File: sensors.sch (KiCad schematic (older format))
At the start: 4 parts

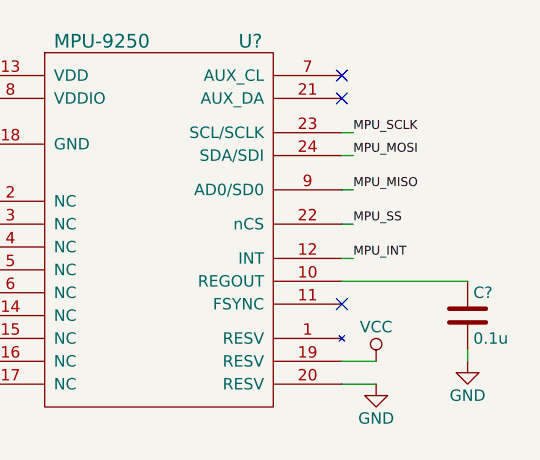
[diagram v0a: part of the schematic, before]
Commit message: Adjust MPU9250 wiring to MCU
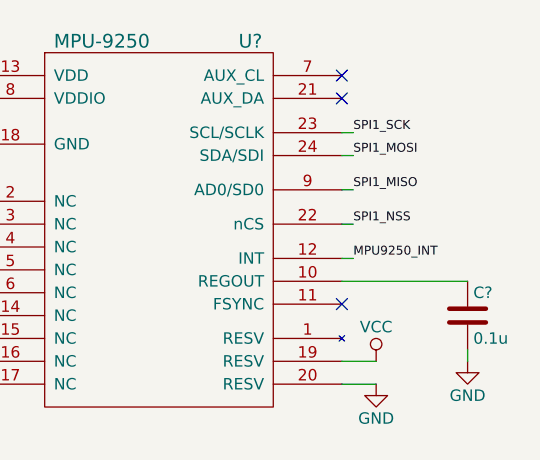
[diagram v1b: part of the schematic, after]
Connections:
- net MPU_INT renamed MPU9250_INT
- net MPU_MISO renamed SPI1_MISO
- net MPU_MOSI renamed SPI1_MOSI
- net MPU_SCLK renamed SPI1_SCK
- net MPU_SS renamed SPI1_NSS
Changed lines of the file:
@@
 $EndComp
 Text Label 3750 1950 0    39   ~ 0
-MPU_MISO
+SPI1_MISO
 Wire Wire Line
 	2100 2800 1900 2800
@@
 	3750 1950 3700 1950
 Text Label 3750 2100 0    39   ~ 0
-MPU_SS
+SPI1_NSS
 Wire Wire Line
 	3750 2100 3700 2100
 Text Label 3750 1800 0    39   ~ 0
-MPU_MOSI
+SPI1_MOSI
 Text Label 3750 1700 0    39   ~ 0
-MPU_SCLK
+SPI1_SCK
 Wire Wire Line
 	3750 1800 3700 1800
@@
 NoConn ~ 3700 2450
 Text Label 3750 2250 0    39   ~ 0
-MPU_INT
+MPU9250_INT
 Wire Wire Line
 	3750 2250 3700 2250

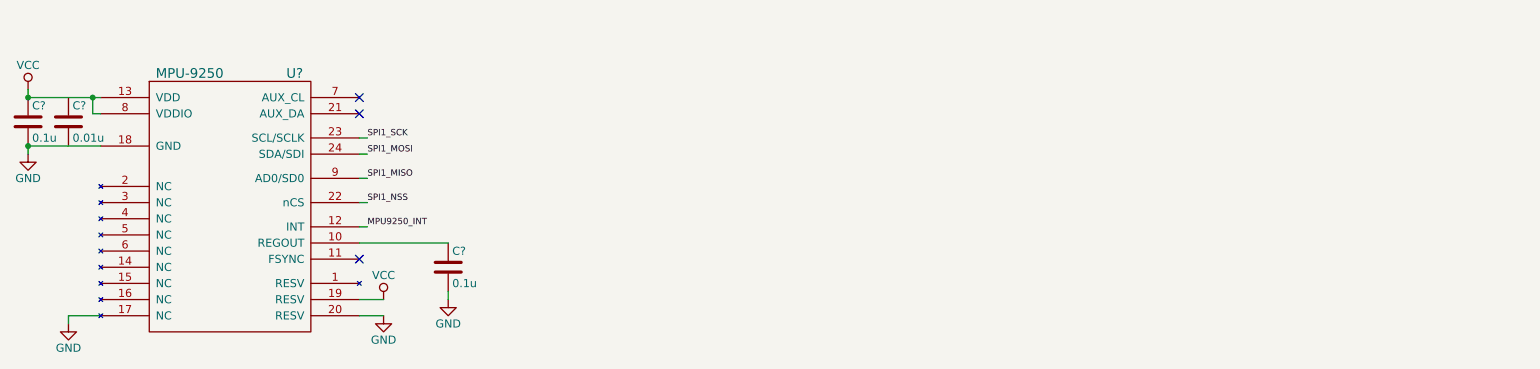
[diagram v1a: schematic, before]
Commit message: Add ground sensor (VL6180X)
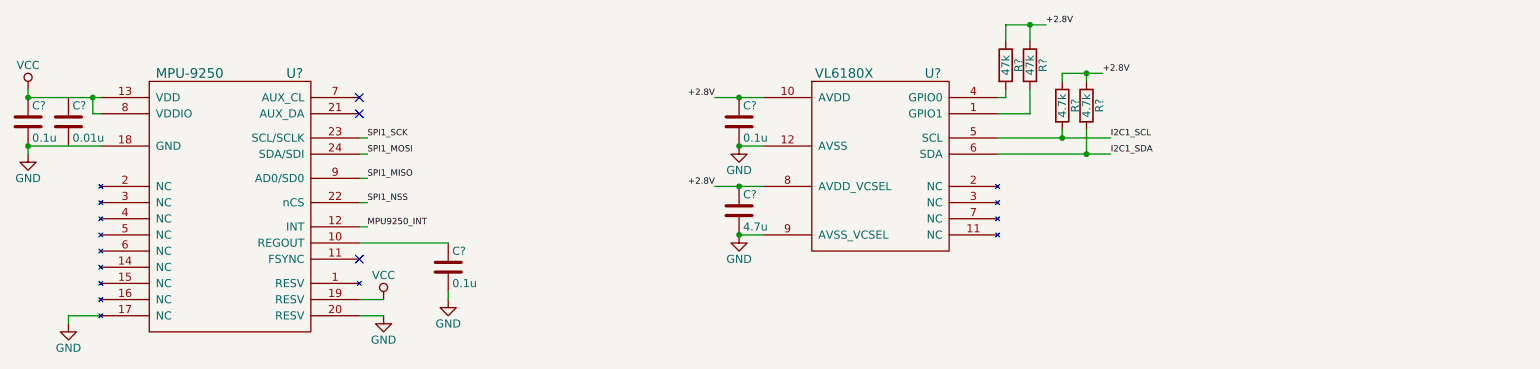
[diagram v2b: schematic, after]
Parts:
- added C?: 4.7u, symbol C
- added C?: 0.1u, symbol C
- added R? (x2): 47k, symbol R
- added R? (x2): 4.7k, symbol R
- added U?: VL6180X, symbol VL6180X
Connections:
- net GND: now also C?.2, C?.2, U?.12 (AVSS), U?.9 (AVSS_VCSEL)
- new net: R?.2, U?.4 (GPIO0)
- new net: R?.2, U?.1 (GPIO1)
- new net +2.8V: C?.1, C?.1, R?.1, R?.1, R?.1, R?.1, U?.10 (AVDD), U?.8 (AVDD_VCSEL)
- new net I2C1_SCL: R?.2, U?.5 (SCL)
- new net I2C1_SDA: R?.2, U?.6 (SDA)
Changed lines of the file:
@@
 Text Label 3750 1950 0    39   ~ 0
 SPI1_MISO
-Wire Wire Line
-	2100 2800 1900 2800
-Wire Wire Line
-	1900 2800 1900 2850
-Wire Wire Line
-	1650 1450 2100 1450
-Wire Wire Line
-	1650 1750 2100 1750
-Wire Wire Line
-	1650 1450 1650 1400
-Wire Wire Line
-	1650 1750 1650 1800
-Connection ~ 1650 1750
-Connection ~ 1650 1450
-Connection ~ 2050 1450
-Wire Wire Line
-	2100 1550 2050 1550
-Wire Wire Line
-	2050 1550 2050 1450
-Wire Wire Line
-	4250 2700 4250 2650
-Wire Wire Line
-	4250 2350 3700 2350
-Wire Wire Line
-	3750 1950 3700 1950
 Text Label 3750 2100 0    39   ~ 0
 SPI1_NSS
-Wire Wire Line
-	3750 2100 3700 2100
 Text Label 3750 1800 0    39   ~ 0
 SPI1_MOSI
 Text Label 3750 1700 0    39   ~ 0
 SPI1_SCK
-Wire Wire Line
-	3750 1800 3700 1800
-Wire Wire Line
-	3750 1700 3700 1700
 NoConn ~ 3700 1450
 NoConn ~ 3700 1550
@@
 Text Label 3750 2250 0    39   ~ 0
 MPU9250_INT
-Wire Wire Line
-	3750 2250 3700 2250
 $Comp
 L MPU-9250 U?
@@
 	1    0    0    -1
 $EndComp
+Text Label 5900 1450 2    39   ~ 0
++2.8V
+Text Label 5900 2000 2    39   ~ 0
++2.8V
+Wire Wire Line
+	2100 2800 1900 2800
+Wire Wire Line
+	1900 2800 1900 2850
+Wire Wire Line
+	1650 1450 2050 1450
+Wire Wire Line
+	2050 1450 2100 1450
+Wire Wire Line
+	1650 1750 2100 1750
+Wire Wire Line
+	1650 1450 1650 1400
+Wire Wire Line
+	1650 1750 1650 1800
+Connection ~ 1650 1750
+Connection ~ 1650 1450
+Connection ~ 2050 1450
+Wire Wire Line
+	2100 1550 2050 1550
+Wire Wire Line
+	2050 1550 2050 1450
+Wire Wire Line
+	4250 2700 4250 2650
+Wire Wire Line
+	4250 2350 3700 2350
+Wire Wire Line
+	3750 1950 3700 1950
+Wire Wire Line
+	3750 2100 3700 2100
+Wire Wire Line
+	3750 1800 3700 1800
+Wire Wire Line
+	3750 1700 3700 1700
+Wire Wire Line
+	3750 2250 3700 2250
 Wire Wire Line
 	3850 2800 3700 2800
 Wire Wire Line
 	3700 2700 3850 2700
+Wire Wire Line
+	5900 1450 6050 1450
+Wire Wire Line
+	6050 1450 6200 1450
+Wire Wire Line
+	5900 2000 6050 2000
+Wire Wire Line
+	6050 2000 6200 2000
+$Comp
+L C C?
+U 1 1 5536FB84
+P 6050 2150
+F 0 "C?" H 6075 2250 50  0000 L CNN
+F 1 "4.7u" H 6075 2050 50  0000 L CNN
+F 2 "" H 6088 2000 30  0000 C CNN
+F 3 "" H 6050 2150 60  0000 C CNN
+	1    6050 2150
+	1    0    0    -1
+$EndComp
+Wire Wire Line
+	6050 2300 6200 2300
+$Comp
+L GND #PWR?
+U 1 1 5536FBED
+P 6050 2300
+F 0 "#PWR?" H 6050 2050 50  0001 C CNN
+F 1 "GND" H 6050 2150 50  0000 C CNN
+F 2 "" H 6050 2300 60  0000 C CNN
+F 3 "" H 6050 2300 60  0000 C CNN
+	1    6050 2300
+	1    0    0    -1
+$EndComp
+$Comp
+L GND #PWR?
+U 1 1 5536FC2A
+P 6050 1750
+F 0 "#PWR?" H 6050 1500 50  0001 C CNN
+F 1 "GND" H 6050 1600 50  0000 C CNN
+F 2 "" H 6050 1750 60  0000 C CNN
+F 3 "" H 6050 1750 60  0000 C CNN
+	1    6050 1750
+	1    0    0    -1
+$EndComp
+Connection ~ 6050 2300
+Connection ~ 6050 2000
+$Comp
+L C C?
+U 1 1 5536FC5F
+P 6050 1600
+F 0 "C?" H 6075 1700 50  0000 L CNN
+F 1 "0.1u" H 6075 1500 50  0000 L CNN
+F 2 "" H 6088 1450 30  0000 C CNN
+F 3 "" H 6050 1600 60  0000 C CNN
+	1    6050 1600
+	1    0    0    -1
+$EndComp
+Wire Wire Line
+	6200 1750 6050 1750
+Connection ~ 6050 1750
+Connection ~ 6050 1450
+$Comp
+L R R?
+U 1 1 5536FCF9
+P 7700 1250
+F 0 "R?" V 7780 1250 50  0000 C CNN
+F 1 "47k" V 7700 1250 50  0000 C CNN
+F 2 "" V 7630 1250 30  0000 C CNN
+F 3 "" H 7700 1250 30  0000 C CNN
+	1    7700 1250
+	1    0    0    -1
+$EndComp
+$Comp
+L R R?
+U 1 1 5536FD36
+P 7850 1250
+F 0 "R?" V 7930 1250 50  0000 C CNN
+F 1 "47k" V 7850 1250 50  0000 C CNN
+F 2 "" V 7780 1250 30  0000 C CNN
+F 3 "" H 7850 1250 30  0000 C CNN
+	1    7850 1250
+	1    0    0    -1
+$EndComp
+Text Label 7950 1000 0    39   ~ 0
++2.8V
+Wire Wire Line
+	7700 1000 7850 1000
+Wire Wire Line
+	7850 1000 7950 1000
+Wire Wire Line
+	7850 1000 7850 1100
+Wire Wire Line
+	7700 1000 7700 1100
+Connection ~ 7850 1000
+Wire Wire Line
+	7650 1450 7700 1450
+Wire Wire Line
+	7650 1550 7850 1550
+Wire Wire Line
+	7850 1550 7850 1400
+Text Label 8300 1300 0    39   ~ 0
++2.8V
+$Comp
+L R R?
+U 1 1 5536FF70
+P 8200 1500
+F 0 "R?" V 8280 1500 50  0000 C CNN
+F 1 "4.7k" V 8200 1500 50  0000 C CNN
+F 2 "" V 8130 1500 30  0000 C CNN
+F 3 "" H 8200 1500 30  0000 C CNN
+	1    8200 1500
+	1    0    0    -1
+$EndComp
+Wire Wire Line
+	8050 1300 8200 1300
+Wire Wire Line
+	8200 1300 8300 1300
+Wire Wire Line
+	8200 1300 8200 1350
+Wire Wire Line
+	8050 1300 8050 1350
+Connection ~ 8200 1300
+Wire Wire Line
+	8050 1650 8050 1700
+Wire Wire Line
+	7650 1700 8050 1700
+Wire Wire Line
+	8050 1700 8350 1700
+Wire Wire Line
+	7650 1800 8200 1800
+Wire Wire Line
+	8200 1800 8350 1800
+Wire Wire Line
+	8200 1800 8200 1650
+Wire Wire Line
+	7700 1450 7700 1400
+Text Label 8350 1700 0    39   ~ 0
+I2C1_SCL
+Text Label 8350 1800 0    39   ~ 0
+I2C1_SDA
+Connection ~ 8200 1800
+Connection ~ 8050 1700
+$Comp
+L VL6180X U?
+U 1 1 553709E6
+P 6600 1700
+F 0 "U?" H 7250 2100 59  0000 C CNN
+F 1 "VL6180X" H 6700 2100 59  0000 C CNN
+F 2 "" H 6800 2300 39  0000 C CNN
+F 3 "" H 6800 2300 39  0000 C CNN
+	1    6600 1700
+	1    0    0    -1
+$EndComp
+$Comp
+L R R?
+U 1 1 5536FEA0
+P 8050 1500
+F 0 "R?" V 8130 1500 50  0000 C CNN
+F 1 "4.7k" V 8050 1500 50  0000 C CNN
+F 2 "" V 7980 1500 30  0000 C CNN
+F 3 "" H 8050 1500 30  0000 C CNN
+	1    8050 1500
+	1    0    0    -1
+$EndComp
 $EndSCHEMATC

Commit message: Add level shifters for i2c of TOF sensor
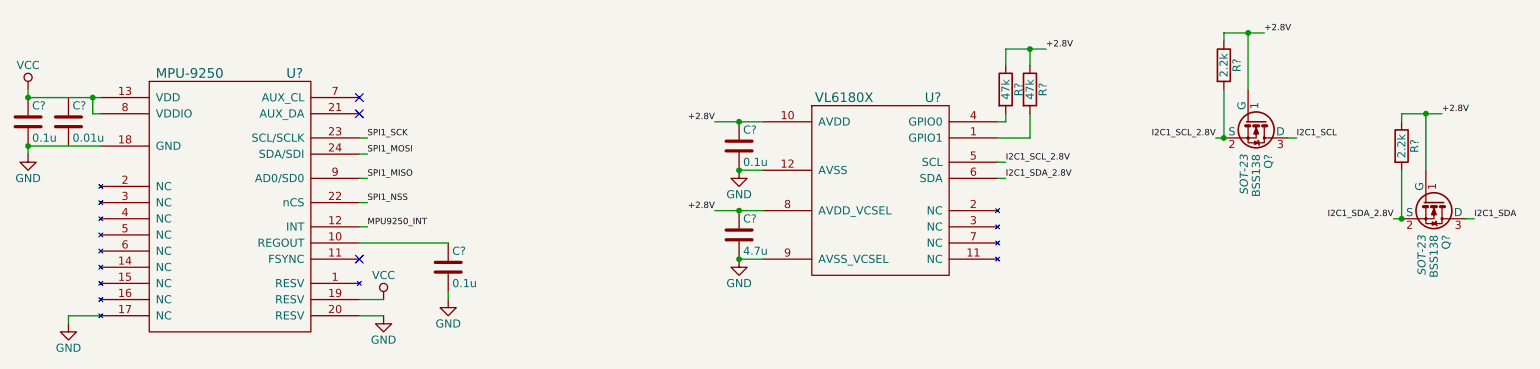
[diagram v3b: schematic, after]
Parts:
- added Q? (x2): BSS138, SOT-23, symbol BSS138
- R? (x2): value 4.7k -> 2.2k
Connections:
- net +2.8V: now also Q?.1 (G), Q?.1 (G)
- net I2C1_SCL: now also Q?.3 (D); no longer R?.2, U?.5 (SCL)
- net I2C1_SDA: now also Q?.3 (D); no longer R?.2, U?.6 (SDA)
- new net I2C1_SCL_2.8V: Q?.2 (S), R?.2, U?.5 (SCL)
- new net I2C1_SDA_2.8V: Q?.2 (S), R?.2, U?.6 (SDA)
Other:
- moved on the sheet: C?, R?, U?
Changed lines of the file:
@@
 	1    0    0    -1
 $EndComp
-Text Label 5900 1450 2    39   ~ 0
-+2.8V
-Text Label 5900 2000 2    39   ~ 0
+Text Label 5900 1600 2    39   ~ 0
++2.8V
+Text Label 5900 2150 2    39   ~ 0
 +2.8V
 Wire Wire Line
@@
 	1900 2800 1900 2850
 Wire Wire Line
-	1650 1450 2050 1450
-Wire Wire Line
-	2050 1450 2100 1450
+	1650 1450 2100 1450
 Wire Wire Line
 	1650 1750 2100 1750
@@
 	3700 2700 3850 2700
 Wire Wire Line
-	5900 1450 6050 1450
-Wire Wire Line
-	6050 1450 6200 1450
-Wire Wire Line
-	5900 2000 6050 2000
-Wire Wire Line
-	6050 2000 6200 2000
+	5900 1600 6200 1600
+Wire Wire Line
+	5900 2150 6200 2150
 $Comp
 L C C?
 U 1 1 5536FB84
-P 6050 2150
-F 0 "C?" H 6075 2250 50  0000 L CNN
-F 1 "4.7u" H 6075 2050 50  0000 L CNN
-F 2 "" H 6088 2000 30  0000 C CNN
-F 3 "" H 6050 2150 60  0000 C CNN
-	1    6050 2150
-	1    0    0    -1
-$EndComp
-Wire Wire Line
-	6050 2300 6200 2300
+P 6050 2300
+F 0 "C?" H 6075 2400 50  0000 L CNN
+F 1 "4.7u" H 6075 2200 50  0000 L CNN
+F 2 "" H 6088 2150 30  0000 C CNN
+F 3 "" H 6050 2300 60  0000 C CNN
+	1    6050 2300
+	1    0    0    -1
+$EndComp
+Wire Wire Line
+	6050 2450 6200 2450
 $Comp
 L GND #PWR?
 U 1 1 5536FBED
-P 6050 2300
-F 0 "#PWR?" H 6050 2050 50  0001 C CNN
-F 1 "GND" H 6050 2150 50  0000 C CNN
-F 2 "" H 6050 2300 60  0000 C CNN
-F 3 "" H 6050 2300 60  0000 C CNN
-	1    6050 2300
+P 6050 2450
+F 0 "#PWR?" H 6050 2200 50  0001 C CNN
+F 1 "GND" H 6050 2300 50  0000 C CNN
+F 2 "" H 6050 2450 60  0000 C CNN
+F 3 "" H 6050 2450 60  0000 C CNN
+	1    6050 2450
 	1    0    0    -1
 $EndComp
@@
 L GND #PWR?
 U 1 1 5536FC2A
+P 6050 1900
+F 0 "#PWR?" H 6050 1650 50  0001 C CNN
+F 1 "GND" H 6050 1750 50  0000 C CNN
+F 2 "" H 6050 1900 60  0000 C CNN
+F 3 "" H 6050 1900 60  0000 C CNN
+	1    6050 1900
+	1    0    0    -1
+$EndComp
+Connection ~ 6050 2450
+Connection ~ 6050 2150
+$Comp
+L C C?
+U 1 1 5536FC5F
 P 6050 1750
-F 0 "#PWR?" H 6050 1500 50  0001 C CNN
-F 1 "GND" H 6050 1600 50  0000 C CNN
-F 2 "" H 6050 1750 60  0000 C CNN
+F 0 "C?" H 6075 1850 50  0000 L CNN
+F 1 "0.1u" H 6075 1650 50  0000 L CNN
+F 2 "" H 6088 1600 30  0000 C CNN
 F 3 "" H 6050 1750 60  0000 C CNN
 	1    6050 1750
 	1    0    0    -1
 $EndComp
-Connection ~ 6050 2300
-Connection ~ 6050 2000
-$Comp
-L C C?
-U 1 1 5536FC5F
-P 6050 1600
-F 0 "C?" H 6075 1700 50  0000 L CNN
-F 1 "0.1u" H 6075 1500 50  0000 L CNN
-F 2 "" H 6088 1450 30  0000 C CNN
-F 3 "" H 6050 1600 60  0000 C CNN
-	1    6050 1600
-	1    0    0    -1
-$EndComp
-Wire Wire Line
-	6200 1750 6050 1750
-Connection ~ 6050 1750
-Connection ~ 6050 1450
+Wire Wire Line
+	6200 1900 6050 1900
+Connection ~ 6050 1900
+Connection ~ 6050 1600
 $Comp
 L R R?
 U 1 1 5536FCF9
-P 7700 1250
-F 0 "R?" V 7780 1250 50  0000 C CNN
-F 1 "47k" V 7700 1250 50  0000 C CNN
-F 2 "" V 7630 1250 30  0000 C CNN
-F 3 "" H 7700 1250 30  0000 C CNN
-	1    7700 1250
+P 7700 1400
+F 0 "R?" V 7780 1400 50  0000 C CNN
+F 1 "47k" V 7700 1400 50  0000 C CNN
+F 2 "" V 7630 1400 30  0000 C CNN
+F 3 "" H 7700 1400 30  0000 C CNN
+	1    7700 1400
 	1    0    0    -1
 $EndComp
@@
 L R R?
 U 1 1 5536FD36
-P 7850 1250
-F 0 "R?" V 7930 1250 50  0000 C CNN
-F 1 "47k" V 7850 1250 50  0000 C CNN
-F 2 "" V 7780 1250 30  0000 C CNN
-F 3 "" H 7850 1250 30  0000 C CNN
-	1    7850 1250
-	1    0    0    -1
-$EndComp
-Text Label 7950 1000 0    39   ~ 0
-+2.8V
-Wire Wire Line
-	7700 1000 7850 1000
-Wire Wire Line
-	7850 1000 7950 1000
-Wire Wire Line
-	7850 1000 7850 1100
-Wire Wire Line
-	7700 1000 7700 1100
-Connection ~ 7850 1000
-Wire Wire Line
-	7650 1450 7700 1450
-Wire Wire Line
-	7650 1550 7850 1550
-Wire Wire Line
-	7850 1550 7850 1400
-Text Label 8300 1300 0    39   ~ 0
+P 7850 1400
+F 0 "R?" V 7930 1400 50  0000 C CNN
+F 1 "47k" V 7850 1400 50  0000 C CNN
+F 2 "" V 7780 1400 30  0000 C CNN
+F 3 "" H 7850 1400 30  0000 C CNN
+	1    7850 1400
+	1    0    0    -1
+$EndComp
+Text Label 7950 1150 0    39   ~ 0
++2.8V
+Wire Wire Line
+	7700 1150 7950 1150
+Wire Wire Line
+	7850 1150 7850 1250
+Wire Wire Line
+	7700 1150 7700 1250
+Connection ~ 7850 1150
+Wire Wire Line
+	7650 1600 7700 1600
+Wire Wire Line
+	7650 1700 7850 1700
+Wire Wire Line
+	7850 1700 7850 1550
+Text Label 9300 1050 0    39   ~ 0
 +2.8V
 $Comp
 L R R?
 U 1 1 5536FF70
-P 8200 1500
-F 0 "R?" V 8280 1500 50  0000 C CNN
-F 1 "4.7k" V 8200 1500 50  0000 C CNN
-F 2 "" V 8130 1500 30  0000 C CNN
-F 3 "" H 8200 1500 30  0000 C CNN
-	1    8200 1500
-	1    0    0    -1
-$EndComp
-Wire Wire Line
-	8050 1300 8200 1300
-Wire Wire Line
-	8200 1300 8300 1300
-Wire Wire Line
-	8200 1300 8200 1350
-Wire Wire Line
-	8050 1300 8050 1350
-Connection ~ 8200 1300
-Wire Wire Line
-	8050 1650 8050 1700
-Wire Wire Line
-	7650 1700 8050 1700
-Wire Wire Line
-	8050 1700 8350 1700
-Wire Wire Line
-	7650 1800 8200 1800
-Wire Wire Line
-	8200 1800 8350 1800
-Wire Wire Line
-	8200 1800 8200 1650
-Wire Wire Line
-	7700 1450 7700 1400
-Text Label 8350 1700 0    39   ~ 0
-I2C1_SCL
-Text Label 8350 1800 0    39   ~ 0
-I2C1_SDA
-Connection ~ 8200 1800
-Connection ~ 8050 1700
+P 10150 1750
+F 0 "R?" V 10230 1750 50  0000 C CNN
+F 1 "2.2k" V 10150 1750 50  0000 C CNN
+F 2 "" V 10080 1750 30  0000 C CNN
+F 3 "" H 10150 1750 30  0000 C CNN
+	1    10150 1750
+	1    0    0    -1
+$EndComp
+Wire Wire Line
+	7650 1850 7700 1850
+Wire Wire Line
+	7650 1950 7700 1950
+Wire Wire Line
+	7700 1600 7700 1550
+Text Label 7700 1850 0    39   ~ 0
+I2C1_SCL_2.8V
+Text Label 7700 1950 0    39   ~ 0
+I2C1_SDA_2.8V
 $Comp
 L VL6180X U?
 U 1 1 553709E6
-P 6600 1700
-F 0 "U?" H 7250 2100 59  0000 C CNN
-F 1 "VL6180X" H 6700 2100 59  0000 C CNN
-F 2 "" H 6800 2300 39  0000 C CNN
-F 3 "" H 6800 2300 39  0000 C CNN
-	1    6600 1700
+P 6600 1850
+F 0 "U?" H 7250 2250 59  0000 C CNN
+F 1 "VL6180X" H 6700 2250 59  0000 C CNN
+F 2 "" H 6800 2450 39  0000 C CNN
+F 3 "" H 6800 2450 39  0000 C CNN
+	1    6600 1850
 	1    0    0    -1
 $EndComp
@@
 L R R?
 U 1 1 5536FEA0
-P 8050 1500
-F 0 "R?" V 8130 1500 50  0000 C CNN
-F 1 "4.7k" V 8050 1500 50  0000 C CNN
-F 2 "" V 7980 1500 30  0000 C CNN
-F 3 "" H 8050 1500 30  0000 C CNN
-	1    8050 1500
-	1    0    0    -1
-$EndComp
+P 9050 1250
+F 0 "R?" V 9130 1250 50  0000 C CNN
+F 1 "2.2k" V 9050 1250 50  0000 C CNN
+F 2 "" V 8980 1250 30  0000 C CNN
+F 3 "" H 9050 1250 30  0000 C CNN
+	1    9050 1250
+	1    0    0    -1
+$EndComp
+$Comp
+L BSS138 Q?
+U 1 1 5537886E
+P 9250 1600
+F 0 "Q?" H 9450 1675 50  0000 L CNN
+F 1 "BSS138" H 9450 1600 50  0000 L CNN
+F 2 "SOT-23" H 9450 1525 50  0000 L CIN
+F 3 "" H 9250 1600 50  0000 L CNN
+	1    9250 1600
+	0    1    1    0
+$EndComp
+$Comp
+L BSS138 Q?
+U 1 1 553788BF
+P 10350 2100
+F 0 "Q?" H 10550 2175 50  0000 L CNN
+F 1 "BSS138" H 10550 2100 50  0000 L CNN
+F 2 "SOT-23" H 10550 2025 50  0000 L CIN
+F 3 "" H 10350 2100 50  0000 L CNN
+	1    10350 2100
+	0    1    1    0
+$EndComp
+Text Label 9000 1700 2    39   ~ 0
+I2C1_SCL_2.8V
+Text Label 10100 2200 2    39   ~ 0
+I2C1_SDA_2.8V
+Wire Wire Line
+	9000 1700 9050 1700
+Wire Wire Line
+	10100 2200 10150 2200
+Wire Wire Line
+	9050 1700 9050 1400
+Connection ~ 9050 1700
+Wire Wire Line
+	9200 1400 9200 1050
+Wire Wire Line
+	9050 1050 9300 1050
+Wire Wire Line
+	9050 1050 9050 1100
+Connection ~ 9200 1050
+Wire Wire Line
+	10150 1600 10150 1550
+Wire Wire Line
+	10150 1550 10400 1550
+Wire Wire Line
+	10300 1550 10300 1900
+Wire Wire Line
+	10150 2200 10150 1900
+Connection ~ 10150 2200
+Connection ~ 10300 1550
+Text Label 10400 1550 0    39   ~ 0
++2.8V
+Text Label 9500 1700 0    39   ~ 0
+I2C1_SCL
+Wire Wire Line
+	9500 1700 9450 1700
+Text Label 10600 2200 0    39   ~ 0
+I2C1_SDA
+Wire Wire Line
+	10600 2200 10550 2200
 $EndSCHEMATC
